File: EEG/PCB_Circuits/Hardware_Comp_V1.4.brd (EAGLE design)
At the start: 109.2 x 51.7 mm, 34 parts, among them U1 AD8422ARMZRM_8-L, U2 LMV324, U3 LMV324, U4 LMV324

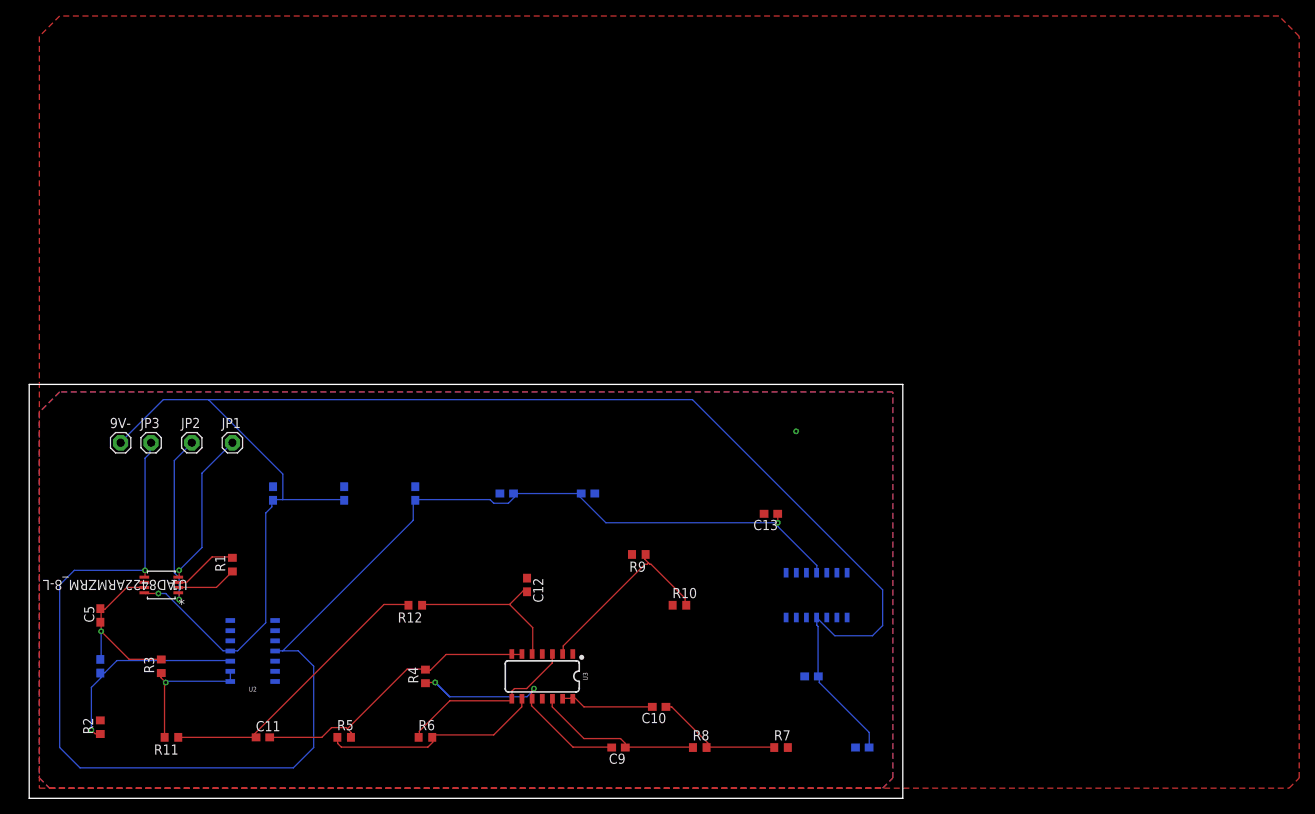
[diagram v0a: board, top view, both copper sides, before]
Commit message: fixed polygon
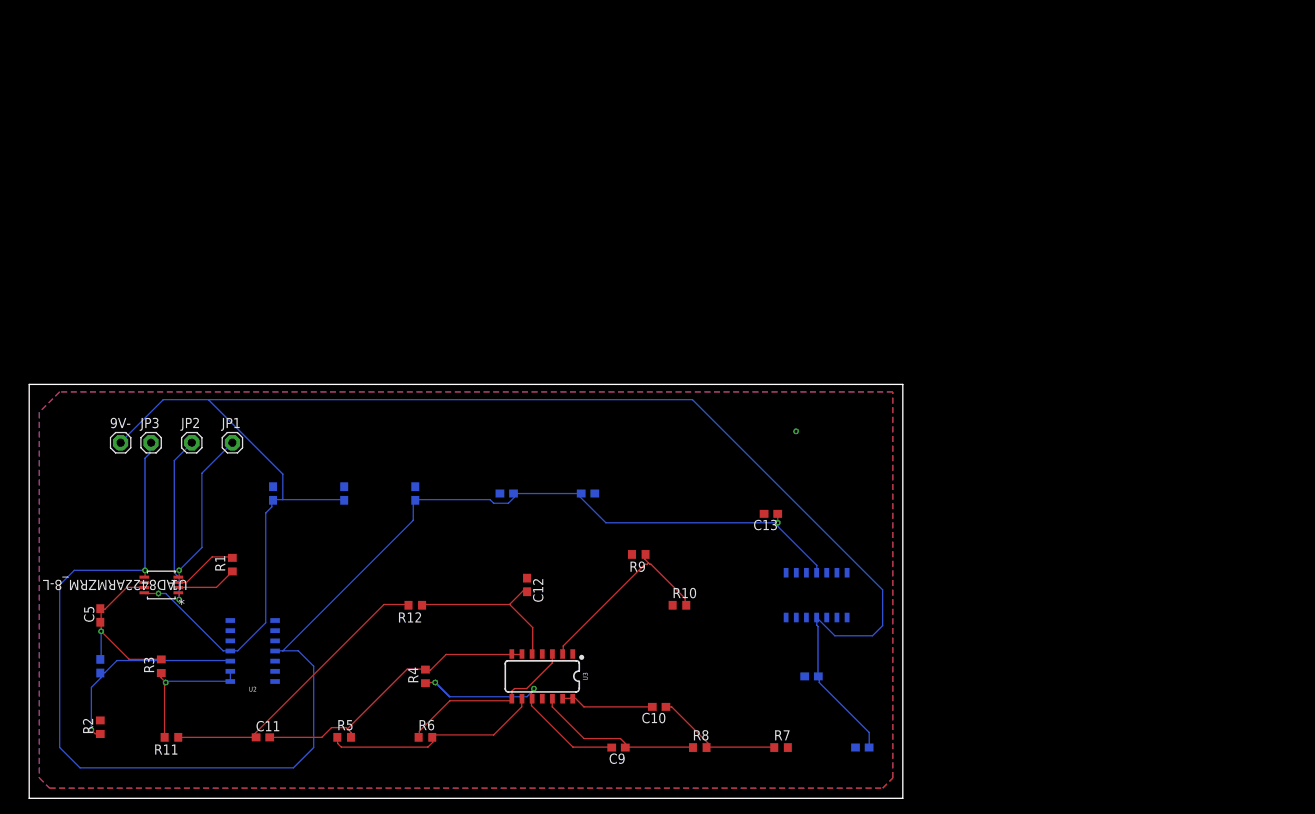
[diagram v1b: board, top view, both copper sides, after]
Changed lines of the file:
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@@
 <contactref element="C8" pad="2"/>
 <contactref element="C13" pad="2"/>
-<polygon width="0.1524" layer="1">
-<vertex x="3.81" y="97.79"/>
-<vertex x="1.27" y="95.25"/>
-<vertex x="1.27" y="1.27"/>
-<vertex x="157.48" y="1.27"/>
-<vertex x="158.75" y="2.54"/>
-<vertex x="158.75" y="95.25"/>
-<vertex x="156.21" y="97.79"/>
-</polygon>
 <polygon width="0.1524" layer="16">
 <vertex x="3.81" y="50.8"/>
@@
 </polygon>
 <via x="95.8596" y="45.8724" extent="1-16" drill="0.35"/>
+<wire x1="91.86" y1="35.56" x2="95.8596" y2="45.8724" width="0" layer="19" extent="1-1"/>
+<wire x1="75.35" y1="30.48" x2="91.86" y2="35.56" width="0" layer="19" extent="1-1"/>
+<wire x1="70.7" y1="38.1" x2="75.35" y2="30.48" width="0" layer="19" extent="1-16"/>
+<wire x1="58.84" y1="38.1" x2="70.7" y2="38.1" width="0" layer="19" extent="16-16"/>
+<wire x1="48.26" y1="38.95" x2="58.84" y2="38.1" width="0" layer="19" extent="16-16"/>
+<wire x1="39.37" y1="38.95" x2="48.26" y2="38.95" width="0" layer="19" extent="16-16"/>
+<wire x1="30.48" y1="38.95" x2="39.37" y2="38.95" width="0" layer="19" extent="16-16"/>
+<wire x1="62.23" y1="27.52" x2="58.84" y2="38.1" width="0" layer="19" extent="1-16"/>
+<wire x1="14.3891" y1="26.995" x2="30.48" y2="38.95" width="0" layer="19" extent="1-16"/>
+<wire x1="8.89" y1="9.74" x2="14.3891" y2="26.995" width="0" layer="19" extent="1-1"/>
+<wire x1="96.94" y1="15.24" x2="91.86" y2="35.56" width="0" layer="19" extent="1-16"/>
+<wire x1="94.83" y1="6.35" x2="96.94" y2="15.24" width="0" layer="19" extent="1-16"/>
+<wire x1="103.29" y1="6.35" x2="94.83" y2="6.35" width="0" layer="19" extent="1-16"/>
 </signal>
 <signal name="N$1">
